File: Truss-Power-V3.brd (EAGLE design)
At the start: 40.3 x 20.3 mm, 31 parts, among them J1 XF2L-0535-1, U1 TPS61090, U2 MCP73831T-2ACI/OT, U3 MAX17044, X1 22-23-2021, X2 MicroB, X3 22-23-2021, X4 CON-1PIN

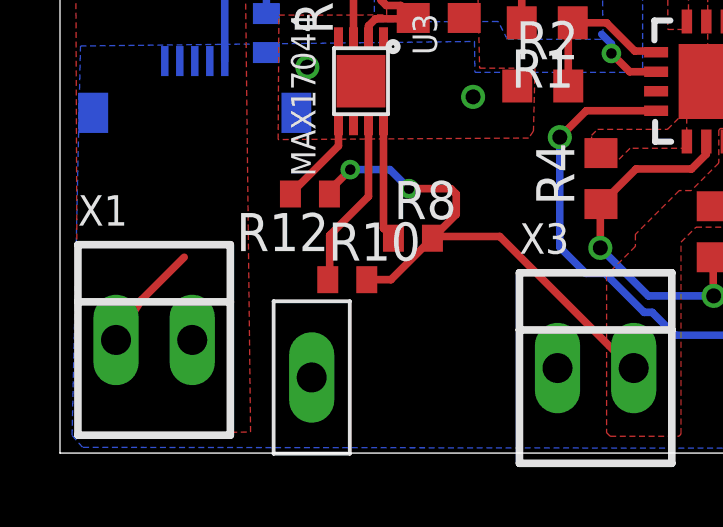
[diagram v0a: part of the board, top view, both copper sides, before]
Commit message: v3 truss power battery connector updated
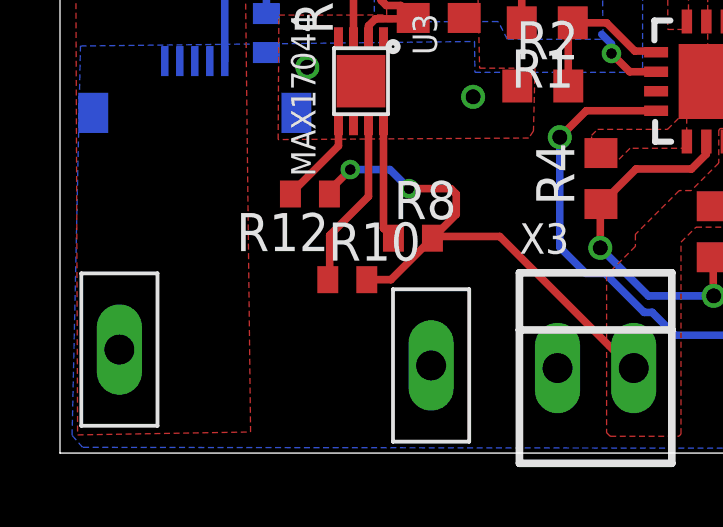
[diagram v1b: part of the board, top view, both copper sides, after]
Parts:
- removed X1: 22-23-2021, con-molex:22-23-2021
- added X5: CON-1PIN, NewPart:CON-1PIN
- moved X4 6.48 mm to (1.98, 3.45)
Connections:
- net GND: now also X5.P$1; no longer X1.2
- net VBAT: now also X4.P$1; no longer X1.1
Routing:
- net VBAT: track 10.7 -> 7.08 mm
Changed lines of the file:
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@@
 <?xml version="1.0" encoding="utf-8"?>
 <!DOCTYPE eagle SYSTEM "eagle.dtd">
-<eagle version="8.3.2">
+<eagle version="8.4.3">
 <drawing>
 <settings>
@@
 <param name="dpMaxLengthDifference" value="10mm"/>
 <param name="dpGapFactor" value="2.5"/>
-<param name="checkGrid" value="0"/>
 <param name="checkAngle" value="0"/>
 <param name="checkFont" value="1"/>
 <param name="checkRestrict" value="0"/>
+<param name="checkStop" value="0"/>
 <param name="useDiameter" value="13"/>
 <param name="maxErrors" value="50"/>
@@
 <element name="C4" library="NewPart" package="7343-METRIC" value="100uF" x="27.686" y="6.35" rot="R270"/>
 <element name="C3" library="microbuilder" package="0805-NO" value="10µF" x="34.036" y="18.796"/>
-<element name="X1" library="con-molex" library_urn="urn:adsk.eagle:library:165" package="22-23-2021" value="22-23-2021" x="3.1378" y="3.7708">
-<attribute name="MF" value="MOLEX" x="3.1378" y="3.7708" size="1.778" layer="27" display="off"/>
-<attribute name="MPN" value="22-23-2021" x="3.1378" y="3.7708" size="1.778" layer="27" display="off"/>
-<attribute name="OC_FARNELL" value="1462926" x="3.1378" y="3.7708" size="1.778" layer="27" display="off"/>
-<attribute name="OC_NEWARK" value="25C3832" x="3.1378" y="3.7708" size="1.778" layer="27" display="off"/>
-</element>
 <element name="U3" library="NewPart" package="TDFN" value="MAX17044" x="10.033" y="12.3952" rot="R180"/>
 <element name="R6" library="resistor" package="R0402" value="1K" x="11.0066" y="17.188" rot="R180"/>
@@
 <element name="R13" library="resistor" package="R0402" value="330" x="6.88" y="14" rot="MR90"/>
 <element name="R7" library="resistor" package="R0402" value="470" x="36.66" y="16.97"/>
-<element name="X4" library="NewPart" package="CON-1PIN" value="CON-1PIN" x="8.39" y="2.52" rot="R180"/>
+<element name="X4" library="NewPart" package="CON-1PIN" value="CON-1PIN" x="1.98" y="3.45" rot="R180"/>
+<element name="X5" library="NewPart" package="CON-1PIN" value="CON-1PIN" x="12.37" y="2.92" rot="R180"/>
 </elements>
 <signals>
@@
 <vertex x="7.2712" y="10.4504"/>
 </polygon>
-<contactref element="X1" pad="2"/>
 <contactref element="U3" pad="9"/>
 <contactref element="U3" pad="4"/>
@@
 <wire x1="36.954865625" y1="9.4928" x2="36.654865625" y2="9.1928" width="0.8128" layer="1"/>
 <contactref element="R13" pad="1"/>
+<contactref element="X5" pad="P$1"/>
 </signal>
 <signal name="N$12">
@@
 <vertex x="0.5148" y="19.4774"/>
 </polygon>
-<contactref element="X1" pad="1"/>
 <contactref element="R11" pad="1"/>
-<wire x1="2.7178" y1="5.1054" x2="1.8678" y2="3.7708" width="0.254" layer="1"/>
-<wire x1="2.7178" y1="5.1054" x2="4.1402" y2="6.5278" width="0.254" layer="1"/>
 <via x="15.94" y="17.56" extent="1-16" drill="0.5"/>
 <contactref element="R6" pad="1"/>
@@
 <wire x1="18.380925" y1="13.320925" x2="18.380925" y2="13.639075" width="0.254" layer="16"/>
 <wire x1="18.380925" y1="13.639075" x2="18.06" y2="13.96" width="0.254" layer="16"/>
+<contactref element="X4" pad="P$1"/>
 <wire x1="7.1882" y1="17.0584" x2="4.9926" y2="13.0658" width="0" layer="19" extent="1-16"/>
 </signal>

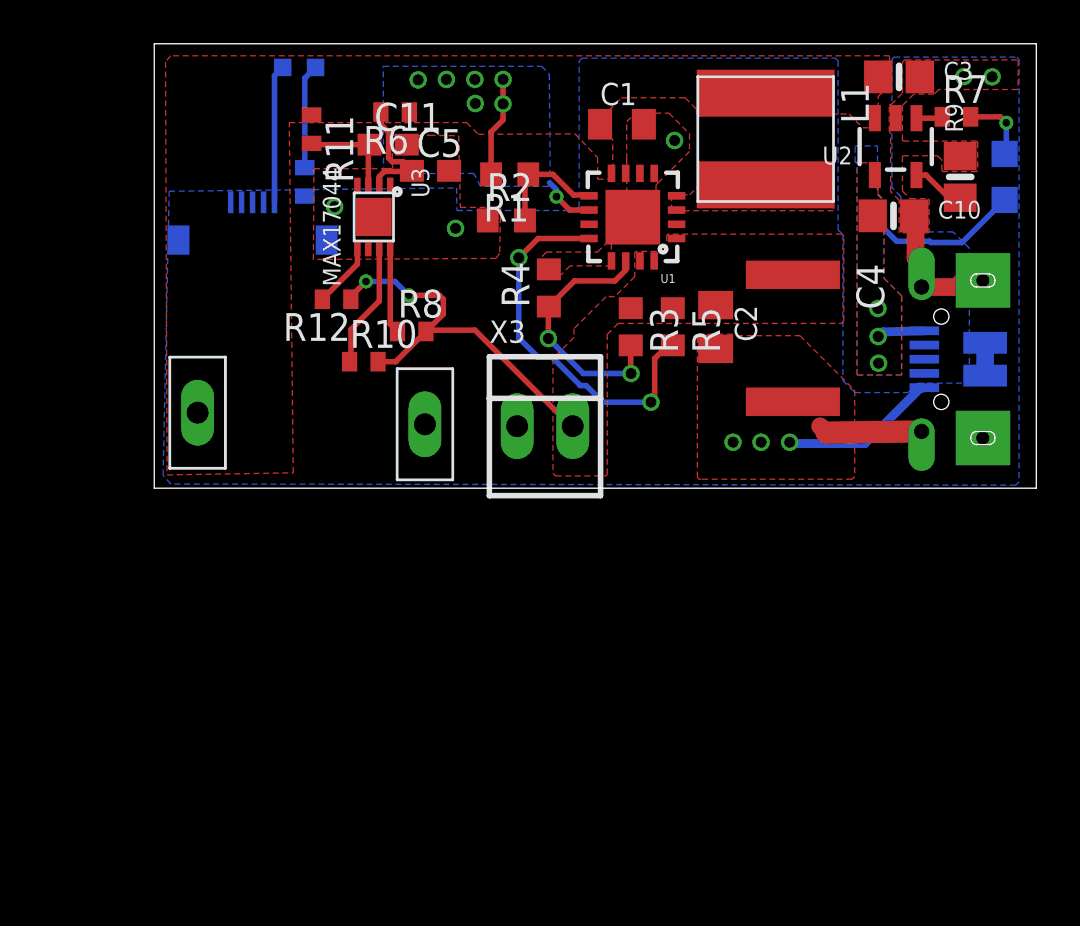
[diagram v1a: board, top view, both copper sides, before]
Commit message: 6-Pin FPC updated.
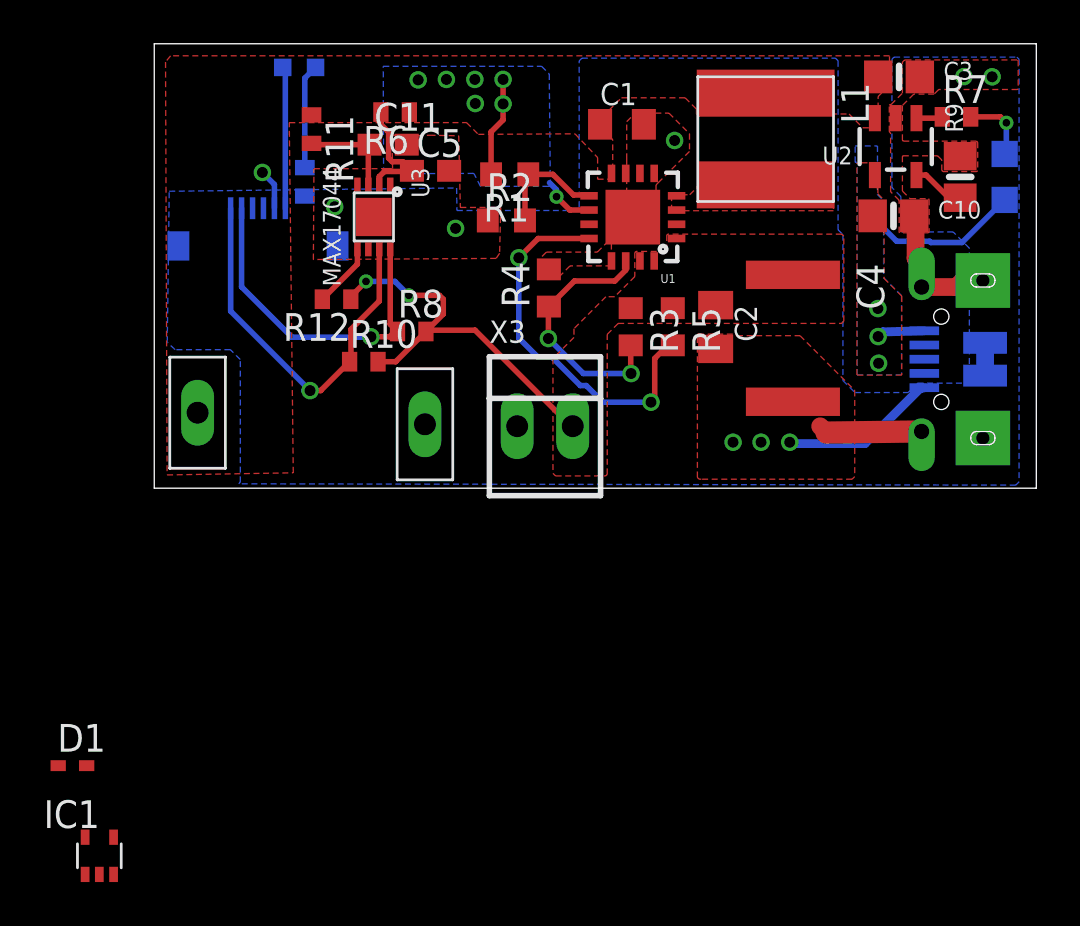
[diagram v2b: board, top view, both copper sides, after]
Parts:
- added D1: (no value), diode:SOD523
- added IC1: 74AUC1G06DCK, 74xx-little-us:SC70-5
- J1: value XF2L-0535-1 -> XF2L-0625-1; device con-omron:XF2L-0535-1 -> con-omron:XF2L-0625-1
- moved J1 0.37 mm to (4.74, 10.9)
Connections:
- removed net EN_SIG: J1.5
- removed net EN_SW: J1.3
- new net DETSW_P: J1.4
- new net PWRSW_P: D1.A, J1.3
- net GND: now also IC1.3
- net SCL: now also J1.6
- net SDA: now also J1.5
- net VCC: now also IC1.5
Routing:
- net SCL: track 5.73 -> 18.2 mm, vias 0 -> 1
- net SDA: track 3.92 -> 15.7 mm, vias 0 -> 1
- net VBAT: track 7.08 -> 8.94 mm, vias 7 -> 8
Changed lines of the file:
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@@
 <layer number="37" name="tTest" color="7" fill="1" visible="no" active="yes"/>
 <layer number="38" name="bTest" color="7" fill="1" visible="no" active="yes"/>
-<layer number="39" name="tKeepout" color="4" fill="11" visible="no" active="yes"/>
+<layer number="39" name="tKeepout" color="4" fill="11" visible="yes" active="yes"/>
 <layer number="40" name="bKeepout" color="1" fill="11" visible="no" active="yes"/>
 <layer number="41" name="tRestrict" color="4" fill="10" visible="no" active="yes"/>
@@
 <element name="R10" library="resistor" package="R0402" value="4.7K" x="9.576" y="5.7802"/>
 <element name="C11" library="rcl" package="C0603" value="10nF" x="10.6886" y="15.6986"/>
-<element name="J1" library="con-omron" package="XF2L-0535-1" value="XF2L-0535-1" x="4.4926" y="11.1608" rot="MR90">
-<attribute name="MF" value="" x="4.4926" y="11.1608" size="1.778" layer="28" rot="MR90" display="off"/>
-<attribute name="MPN" value="XF2L-0535-1A" x="4.4926" y="11.1608" size="1.778" layer="28" rot="MR90" display="off"/>
-<attribute name="OC_FARNELL" value="unknown" x="4.4926" y="11.1608" size="1.778" layer="28" rot="MR90" display="off"/>
-<attribute name="OC_NEWARK" value="37M0863" x="4.4926" y="11.1608" size="1.778" layer="28" rot="MR90" display="off"/>
-</element>
 <element name="U1" library="NewPart" package="TPS61090" value="TPS61090" x="21.87" y="12.386" rot="R180"/>
 <element name="X3" library="con-molex" package="22-23-2021" value="22-23-2021" x="17.854" y="2.834">
@@
 <element name="X4" library="NewPart" package="CON-1PIN" value="CON-1PIN" x="1.98" y="3.45" rot="R180"/>
 <element name="X5" library="NewPart" package="CON-1PIN" value="CON-1PIN" x="12.37" y="2.92" rot="R180"/>
+<element name="J1" library="con-omron" library_urn="urn:adsk.eagle:library:167" package="XF2L-0625-1" package3d_urn="urn:adsk.eagle:package:9011/1" value="XF2L-0625-1" x="4.74" y="10.89" rot="MR90">
+<attribute name="MF" value="OMRON COMPONENTS USA" x="4.74" y="10.89" size="1.778" layer="28" rot="MR90" display="off"/>
+<attribute name="MPN" value="XF2L-0625-1" x="4.74" y="10.89" size="1.778" layer="28" rot="MR90" display="off"/>
+<attribute name="OC_FARNELL" value="1536105" x="4.74" y="10.89" size="1.778" layer="28" rot="MR90" display="off"/>
+<attribute name="OC_NEWARK" value="29C7842" x="4.74" y="10.89" size="1.778" layer="28" rot="MR90" display="off"/>
+</element>
+<element name="D1" library="diode" library_urn="urn:adsk.eagle:library:210" package="SOD523" package3d_urn="urn:adsk.eagle:package:43410/1" value="" x="-3.79" y="-12.68"/>
+<element name="IC1" library="74xx-little-us" library_urn="urn:adsk.eagle:library:87" package="SC70-5" package3d_urn="urn:adsk.eagle:package:2483/1" value="74AUC1G06DCK" x="-2.51" y="-16.8"/>
 </elements>
 <signals>
@@
 <vertex x="39.52" y="0.29"/>
 <vertex x="39.37" y="0.14"/>
-<vertex x="0.752" y="0.1908"/>
-<vertex x="0.4034" y="0.5902"/>
+<vertex x="3.86" y="0.2"/>
+<vertex x="3.93" y="0.27"/>
+<vertex x="3.93" y="5.88"/>
+<vertex x="3.4792" y="6.3308"/>
+<vertex x="0.952" y="6.3308"/>
+<vertex x="0.5934" y="6.6702"/>
 <vertex x="0.6828" y="13.569"/>
 </polygon>
@@
 <contactref element="R13" pad="1"/>
 <contactref element="X5" pad="P$1"/>
+<contactref element="IC1" pad="3"/>
+<wire x1="12.37" y1="2.92" x2="-1.86" y2="-17.65" width="0" layer="19" extent="1-1"/>
 </signal>
 <signal name="N$12">
@@
 <via x="15.94" y="17.56" extent="1-16" drill="0.5"/>
 <contactref element="R6" pad="1"/>
-<contactref element="J1" pad="2"/>
 <wire x1="19.87" y1="12.711" x2="18.99085" y2="12.711" width="0.254" layer="1"/>
 <wire x1="18.99085" y1="12.711" x2="18.380925" y2="13.320925" width="0.254" layer="1"/>
@@
 <wire x1="18.380925" y1="13.639075" x2="18.06" y2="13.96" width="0.254" layer="16"/>
 <contactref element="X4" pad="P$1"/>
-<wire x1="7.1882" y1="17.0584" x2="4.9926" y2="13.0658" width="0" layer="19" extent="1-16"/>
+<contactref element="J1" pad="2"/>
+<wire x1="5.49" y1="12.795" x2="5.49" y2="13.88" width="0.254" layer="16"/>
+<wire x1="5.49" y1="13.88" x2="4.94" y2="14.43" width="0.254" layer="16"/>
+<via x="4.94" y="14.43" extent="1-16" drill="0.5"/>
 </signal>
 <signal name="VBUS">
@@
 <wire x1="14.66" y1="7.22" x2="12.4724" y2="7.22" width="0.254" layer="1"/>
 <wire x1="12.4724" y1="7.22" x2="12.3612" y2="7.1088" width="0.254" layer="1"/>
+<contactref element="IC1" pad="5"/>
+<wire x1="10.226" y1="5.7802" x2="-3.16" y2="-15.95" width="0" layer="19" extent="1-1"/>
 </signal>
 <signal name="SCL">
@@
 <wire x1="10.283" y1="8.553" x2="8.99" y2="7.26" width="0.254" layer="1"/>
 <wire x1="8.99" y1="5.8442" x2="8.99" y2="7.26" width="0.254" layer="1"/>
-<wire x1="8.99" y1="5.8442" x2="8.926" y2="5.7802" width="0.254" layer="1"/>
+<wire x1="8.926" y1="5.7802" x2="8.99" y2="5.8442" width="0.254" layer="1"/>
+<contactref element="J1" pad="6"/>
+<wire x1="7.12" y1="4.46" x2="6.83" y2="4.46" width="0.254" layer="16"/>
+<via x="7.12" y="4.46" extent="1-16" drill="0.5"/>
+<wire x1="7.12" y1="4.46" x2="7.6058" y2="4.46" width="0.254" layer="1"/>
+<wire x1="7.6058" y1="4.46" x2="8.926" y2="5.7802" width="0.254" layer="1"/>
+<wire x1="3.49" y1="12.795" x2="3.49" y2="8.09" width="0.254" layer="16"/>
+<wire x1="3.49" y1="8.09" x2="7.12" y2="4.46" width="0.254" layer="16"/>
 </signal>
 <signal name="SDA">
@@
 <contactref element="U3" pad="8"/>
 <wire x1="10.783" y1="10.9452" x2="10.783" y2="7.495" width="0.254" layer="1"/>
-<wire x1="11.1152" y1="7.1628" x2="10.783" y2="7.495" width="0.254" layer="1"/>
+<wire x1="11.054" y1="7.224" x2="11.1152" y2="7.1628" width="0.254" layer="1"/>
+<contactref element="J1" pad="5"/>
+<wire x1="11.054" y1="7.224" x2="10.783" y2="7.495" width="0.254" layer="1"/>
+<wire x1="3.99" y1="12.795" x2="3.99" y2="9.2" width="0.254" layer="16"/>
+<wire x1="3.99" y1="9.2" x2="6.29" y2="6.9" width="0.254" layer="16"/>
+<wire x1="6.29" y1="6.9" x2="9.88" y2="6.9" width="0.254" layer="16"/>
+<wire x1="9.88" y1="6.9" x2="9.9" y2="6.92" width="0.254" layer="16"/>
+<via x="9.9" y="6.92" extent="1-16" drill="0.5"/>
+<wire x1="9.9" y1="6.92" x2="10.75" y2="6.92" width="0.254" layer="1"/>
+<wire x1="10.75" y1="6.92" x2="11.054" y2="7.224" width="0.254" layer="1"/>
 </signal>
 <signal name="LBI">
@@
 </signal>
 <signal name="LEDSOC">
+<contactref element="LED1" pad="A"/>
 <contactref element="J1" pad="1"/>
-<contactref element="LED1" pad="A"/>
-<wire x1="5.4926" y1="13.0658" x2="5.4926" y2="18.8526" width="0.254" layer="16"/>
-<wire x1="5.4926" y1="18.8526" x2="5.87" y2="19.23" width="0.254" layer="16"/>
+<wire x1="5.99" y1="12.795" x2="5.99" y2="19.11" width="0.254" layer="16"/>
+<wire x1="5.99" y1="19.11" x2="5.87" y2="19.23" width="0.254" layer="16"/>
 </signal>
 <signal name="N$4">
@@
 <wire x1="6.88" y1="18.74" x2="7.37" y2="19.23" width="0.254" layer="16"/>
 </signal>
-<signal name="EN_SW">
+<signal name="PWRSW_P">
 <contactref element="J1" pad="3"/>
-</signal>
-<signal name="EN_SIG">
-<contactref element="J1" pad="5"/>
+<contactref element="D1" pad="A"/>
+<wire x1="-3.09" y1="-12.68" x2="4.99" y2="12.795" width="0" layer="19" extent="1-16"/>
+</signal>
+<signal name="DETSW_P">
+<contactref element="J1" pad="4"/>
 </signal>
 </signals>

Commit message: Charger circuitry updated; Inverter and diode-or added for Boost EN
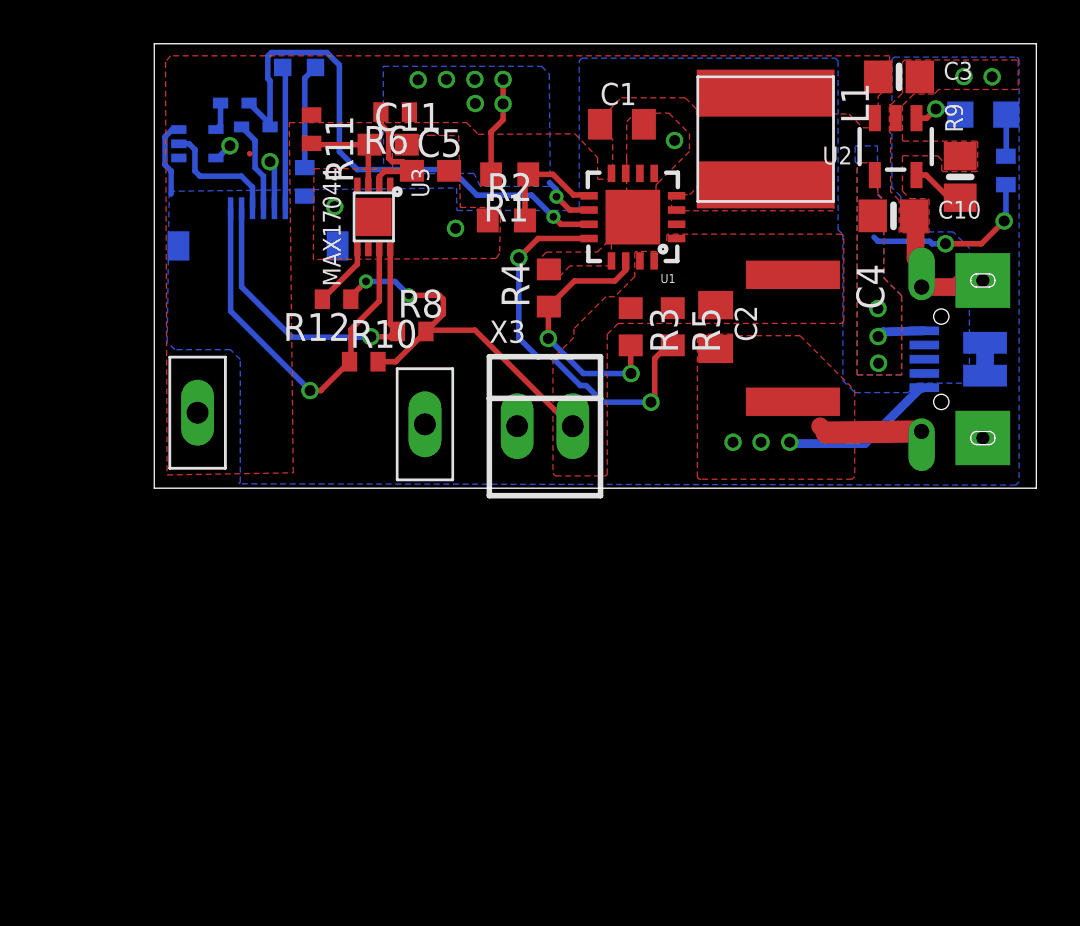
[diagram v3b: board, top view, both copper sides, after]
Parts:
- removed IC1: 74AUC1G06DCK, 74xx-little-us:SC70-5
- added D2: (no value), diode:SOD523
- added U$16: INVERTER-GATE, NewPart:SOC70-5
- moved D1 30.4 mm to (4.69, 16.5), flipped to the bottom
- moved R7 3.33 mm to (38.9, 14.5), flipped to the bottom, turned to 90 degrees
- moved CHRG 3.01 mm to (37.9, 17.1), turned to 270 degrees
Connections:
- removed net N$12: CHRG.C, R7.2
- removed net N$13: R7.1, U2.1
- new net EN_SIG: D1.C, D2.C, U1.11
- new net N$5: D2.A, U$16.4
- new net N$6: CHRG.A, R7.2
- new net N$7: CHRG.C, U2.1
- net DETSW_P: now also U$16.2
- net GND: now also U$16.3; no longer IC1.3
- net VBAT: now also U$16.5
- net VBUS: now also R7.1; no longer CHRG.A
- net VCC: no longer IC1.5
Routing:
- net EN_SIG: track 0.00 -> 25.1 mm, vias 0 -> 1
- net DETSW_P: track 0.00 -> 5.72 mm
- net PWRSW_P: track 0.00 -> 4.13 mm
- net GND: track 19.8 -> 23.3 mm
- net N$12: track 3.20 -> 0.00 mm, vias 1 -> 0
- net N$7: track 0.00 -> 2.68 mm, vias 0 -> 1
- net N$6: track 0.00 -> 1.91 mm
- net N$5: track 0.00 -> 1.30 mm
- net VBAT: track 8.94 -> 10.2 mm, vias 8 -> 9
- net N$13: track 1.20 -> 0.00 mm
- net VBUS: track 9.52 -> 10.4 mm, vias 3 -> 5
